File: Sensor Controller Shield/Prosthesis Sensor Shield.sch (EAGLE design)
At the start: 46 parts, among them M1_ACT M02POLAR_LOCK, M2_ACT M02POLAR_LOCK, U1 74VHC14MTCX, U2 74VHC14MTCX

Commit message: Re-routed motor shield with new molex connectors.
Still may want to put the CCB headers as a better connector, too. Need
to source a good 8x2 pin header first. Added prosthesis logo to motor
board. Added sensor shield schematic (copy of motor board to start)
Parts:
- C6, C7: value 0.1uF -> (none)
- DISP, PRES_INPUT: device SparkFun-Connectors:M04POLAR_LOCK -> SparkFun-Connectors:M04PTH
- M1_ACT, M2_ACT: value M02POLAR_LOCK -> M02PTH; device SparkFun-Connectors:M02POLAR_LOCK -> SparkFun-Connectors:M02PTH
- POT: device SparkFun-Connectors:M06POLAR_LOCK -> SparkFun-Connectors:M06SIP
- R11, R12: value 1M -> (none)
- ROCKERS: device SparkFun-Connectors:M03X2 -> SparkFun-Connectors:M03X22X3_SILK_SM
- renumbered U1 to 74VHC14MTCX, U2 to 74VHC14MTCX1

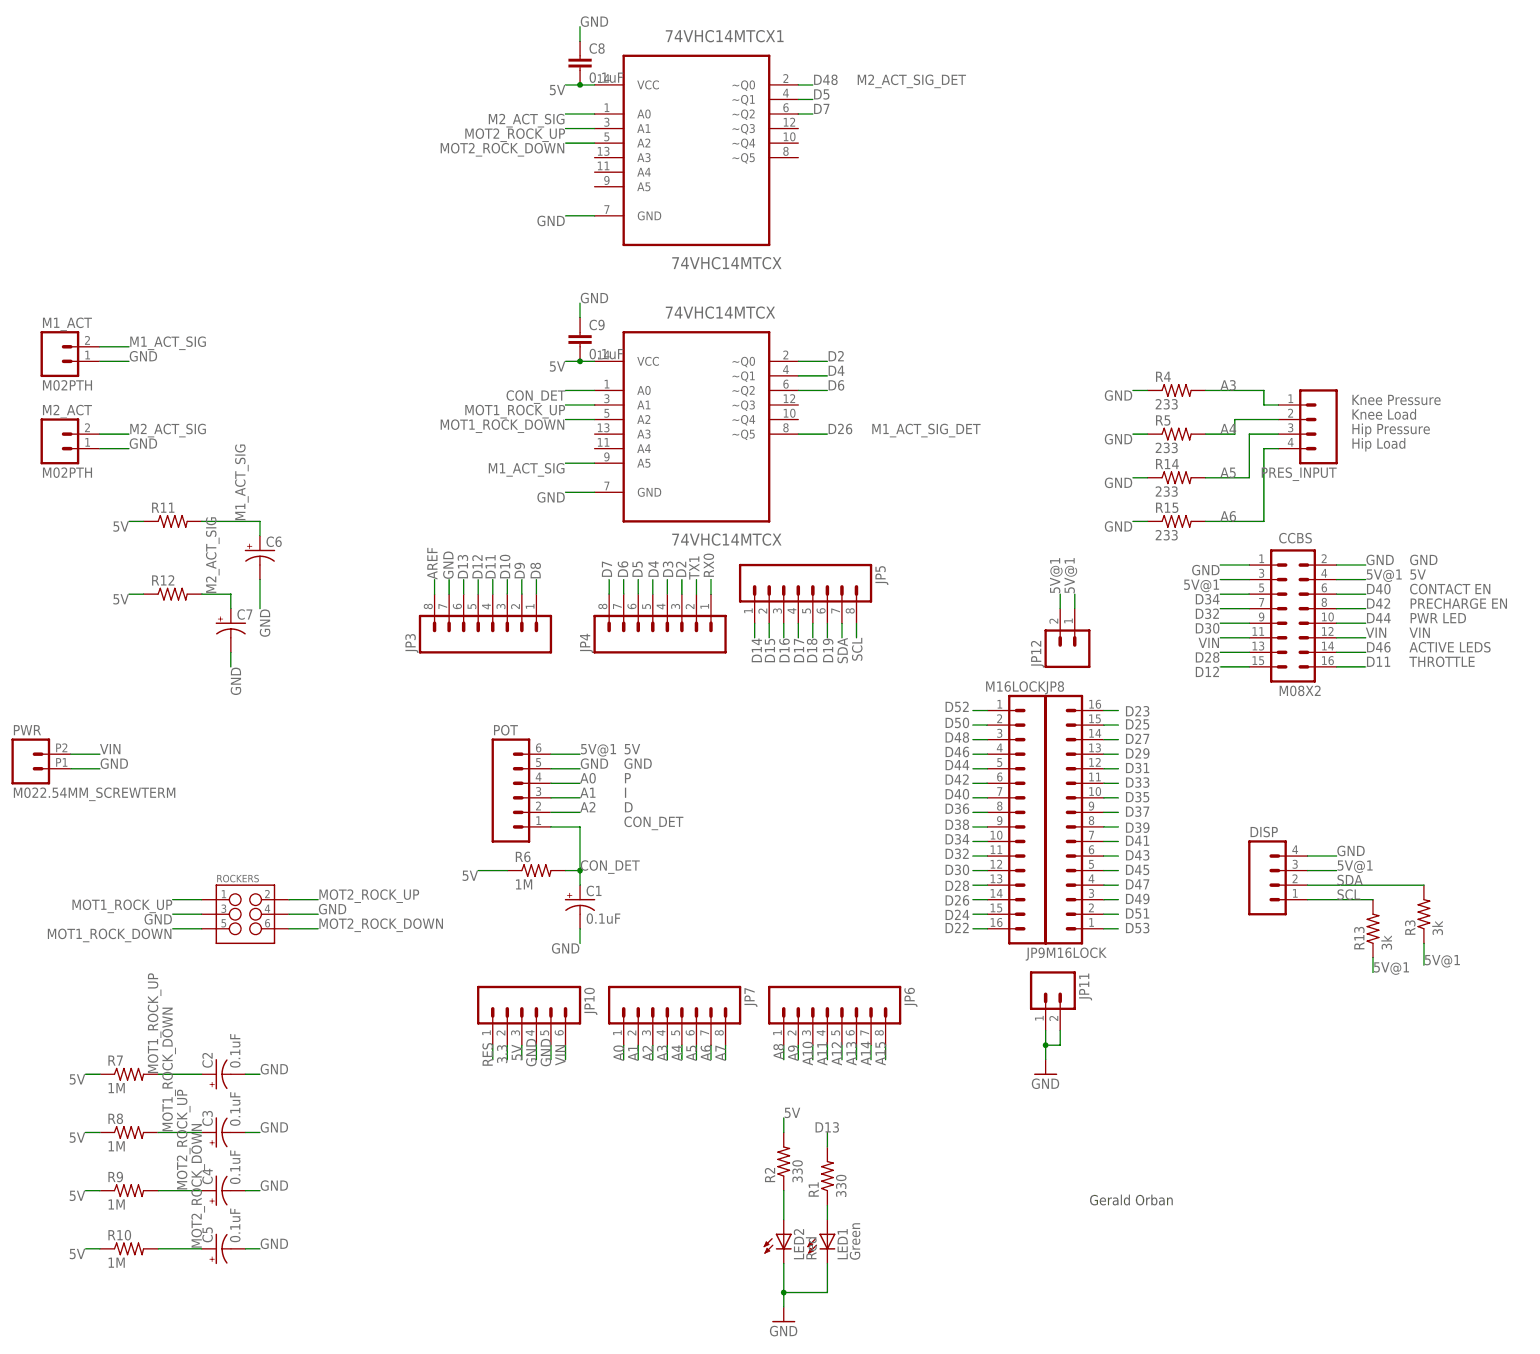
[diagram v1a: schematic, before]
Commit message: Moved MCB titles to places layer from names
Cleared sensor shield of all components
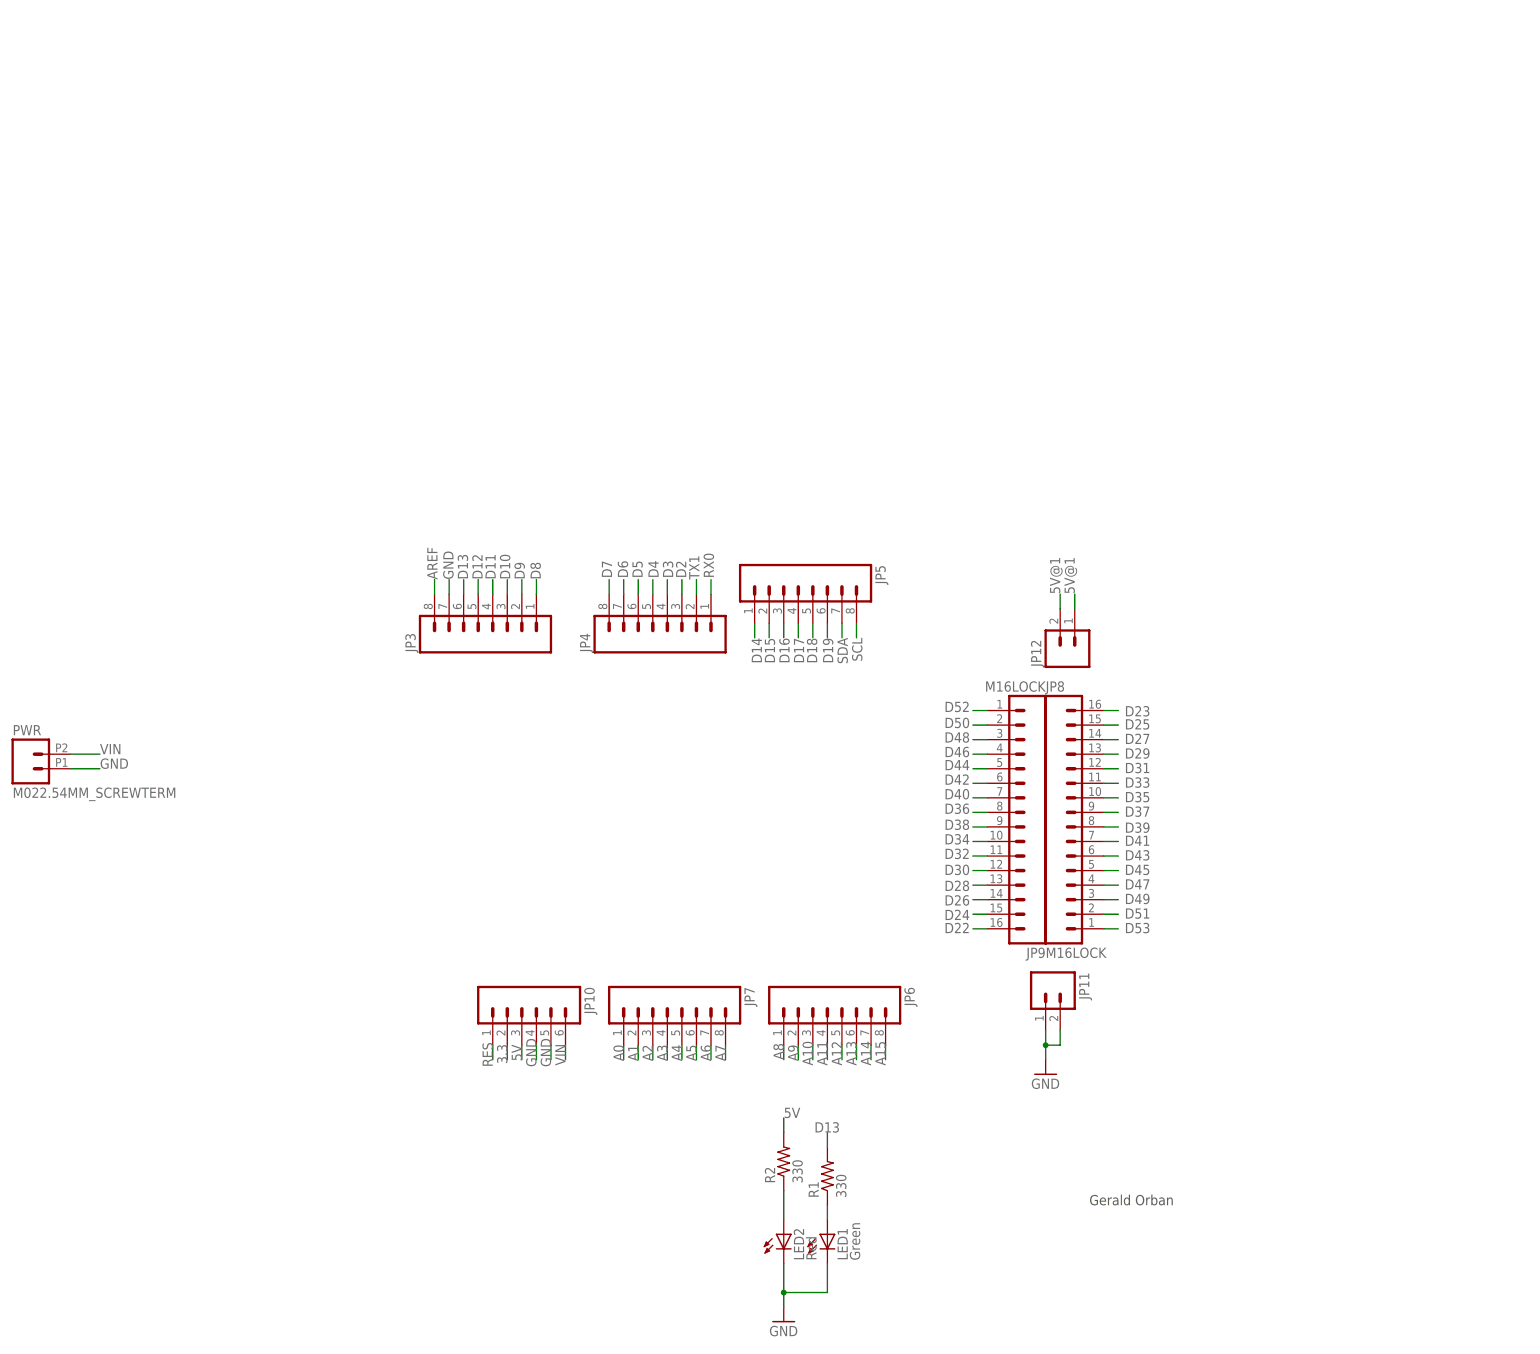
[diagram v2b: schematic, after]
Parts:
- removed 74VHC14MTCX, 74VHC14MTCX1: 74VHC14MTCX, Fairchild_By_element14_Batch_1:74VHC14MTCX
- removed C1, C2, C3, C4, C5: 0.1uF, SparkFun-Capacitors:CAP_POL1206
- removed C6, C7: (no value), SparkFun-Capacitors:CAP_POL1206
- removed C8, C9: 0.1uF, SparkFun-Capacitors:CAP0603-CAP
- removed CCBS: M08X2, SparkFun-Connectors:M08X2
- removed DISP, PRES_INPUT: (no value), SparkFun-Connectors:M04PTH
- removed M1_ACT, M2_ACT: M02PTH, SparkFun-Connectors:M02PTH
- removed POT: (no value), SparkFun-Connectors:M06SIP
- removed R10, R7, R8, R9: 1M, SparkFun-Resistors:RESISTOR0603
- removed R11, R12: (no value), SparkFun-Resistors:RESISTOR0603
- removed R13, R3: 3k, SparkFun-Resistors:RESISTOR0603
- removed R14, R15, R4, R5: 233, SparkFun-Resistors:RESISTORPTH-1/4W
- removed R6: 1M, SparkFun-Resistors:RESISTOR0603-RES
- removed ROCKERS: (no value), SparkFun-Connectors:M03X22X3_SILK_SM
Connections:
- removed net CON_DET: 74VHC14MTCX.A0, C1.+, POT.1, R6.2
- removed net M1_ACT_SIG: 74VHC14MTCX.A5, C6.+, M1_ACT.2, R11.2
- removed net M2_ACT_SIG: 74VHC14MTCX1.A0, C7.+, M2_ACT.2, R12.2
- removed net MOT1_ROCK_DOWN: 74VHC14MTCX.A2, C3.+, R8.2, ROCKERS.5
- removed net MOT1_ROCK_UP: 74VHC14MTCX.A1, C2.+, R7.2, ROCKERS.1
- removed net MOT2_ROCK_DOWN: 74VHC14MTCX1.A2, C5.+, R10.2, ROCKERS.6
- removed net MOT2_ROCK_UP: 74VHC14MTCX1.A1, C4.+, R9.2, ROCKERS.2
- net 5V: no longer 74VHC14MTCX.VCC, 74VHC14MTCX1.VCC, C8.2, C9.2, R10.1, R11.1, R12.1, R6.1, R7.1, R8.1, R9.1
- net 5V@1: no longer CCBS.3, CCBS.4, DISP.3, POT.6, R13.1, R3.1
- net A0: no longer POT.4
- net A1: no longer POT.3
- net A2: no longer POT.2
- net A3: no longer PRES_INPUT.1, R4.2
- net A4: no longer PRES_INPUT.2, R5.2
- net A5: no longer PRES_INPUT.3, R14.2
- net A6: no longer PRES_INPUT.4, R15.2
- net D11: no longer CCBS.16
- net D12: no longer CCBS.15
- net D2: no longer 74VHC14MTCX.~Q0
- net D26: no longer 74VHC14MTCX.~Q5
- net D28: no longer CCBS.13
- net D30: no longer CCBS.9
- net D32: no longer CCBS.7
- net D34: no longer CCBS.5
- net D4: no longer 74VHC14MTCX.~Q1
- net D40: no longer CCBS.6
- net D42: no longer CCBS.8
- net D44: no longer CCBS.10
- net D46: no longer CCBS.14
- net D48: no longer 74VHC14MTCX1.~Q0
- net D5: no longer 74VHC14MTCX1.~Q1
- net D6: no longer 74VHC14MTCX.~Q2
- net D7: no longer 74VHC14MTCX1.~Q2
- net GND: no longer 74VHC14MTCX.GND, 74VHC14MTCX1.GND, C1.-, C2.-, C3.-, C4.-, C5.-, C6.-, C7.-, C8.1, C9.1, CCBS.1, CCBS.2, DISP.4, M1_ACT.1, M2_ACT.1, POT.5, R14.1, R15.1, R4.1, R5.1, ROCKERS.3, ROCKERS.4
- net SCL: no longer DISP.1, R13.2
- net SDA: no longer DISP.2, R3.2
- net VIN: no longer CCBS.11, CCBS.12
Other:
- note removed: "5V"
- note removed: "ACTIVE LEDS"
- note removed: "CONTACT EN"
- note removed: "CON_DET"
- note removed: "D"
- note removed: "GND"
- note removed: "Hip Load"
- note removed: "Hip Pressure"
- note removed: "I"
- note removed: "Knee Load"
- note removed: "Knee Pressure"
- note removed: "M1_ACT_SIG_DET"
- note removed: "M2_ACT_SIG_DET"
- note removed: "P"
- note removed: "PRECHARGE EN"
- note removed: "PWR LED"
- note removed: "THROTTLE"
- note removed: "VIN"
